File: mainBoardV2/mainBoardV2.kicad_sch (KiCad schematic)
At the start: 27 parts, among them J1 USB4125-GF-A_REVA2, U1 ESP32-CAM, U3 MCP73871-2AAI_ML, U4 MPU6050_Module, U5 TPS61023DRLT

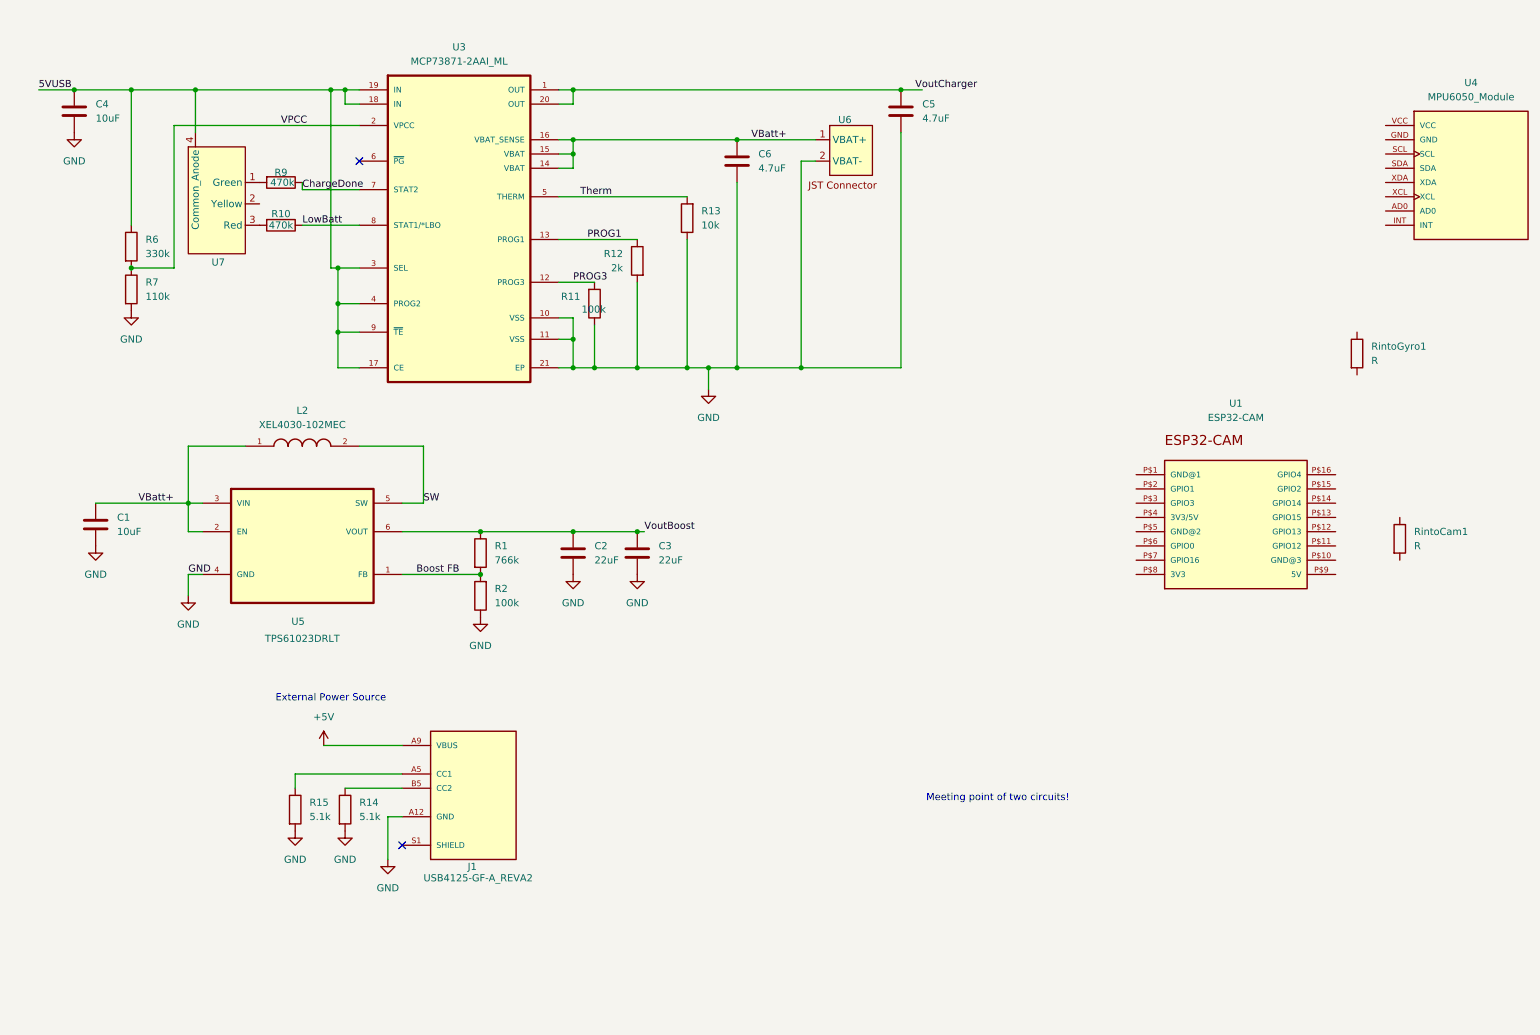
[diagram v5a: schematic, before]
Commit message: 3.11.26.C4
Finalized copper connections and placed ground vias. Got closer to final size goal of 50x50 mm (2x2in). Placed ground vias, and placed thick traces on power connections.
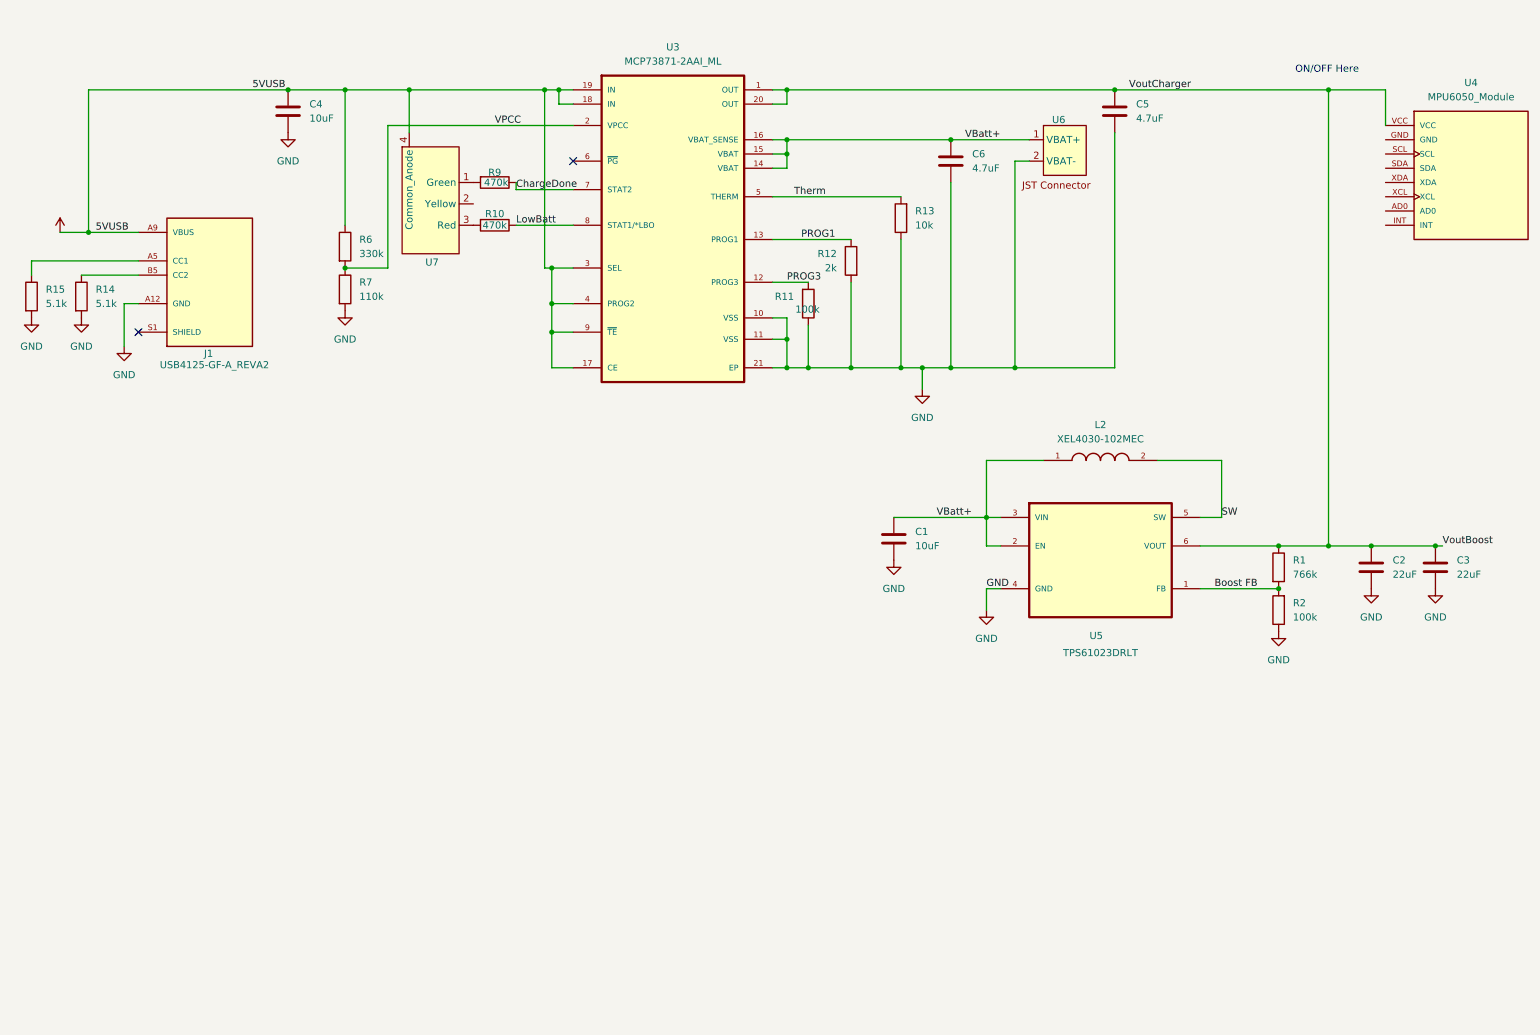
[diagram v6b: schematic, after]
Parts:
- removed RintoCam1, RintoGyro1: R, Resistor_SMD:R_0805_2012Metric_Pad1.20x1.40mm_HandSolder, symbol Device:R
- removed U1: ESP32-CAM, ESP32-CAM:ESP32-CAM, symbol ESP32-CAM:ESP32-CAM
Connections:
- net 5VUSB is gone; now on net +5V: C4.1, R6.1, U3.17 (CE), U3.18 (IN), U3.19 (IN), U3.3 (SEL), U3.4 (PROG2), U3.9 (~{TE}), U7.4 (Common_Anode)
- net VoutCharger is gone; now on net VoutBoost: C5.1, U3.1 (OUT), U3.20 (OUT)
- net VoutBoost: now also U4.VCC
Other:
- note added: "ON/OFF Here"
- note removed: "External Power Source"
- note removed: "Meeting point of two circuits!"
- moved on the sheet: C1, C2, C3, C4, C5, C6, J1, L2, R1, R10, R11, R12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
